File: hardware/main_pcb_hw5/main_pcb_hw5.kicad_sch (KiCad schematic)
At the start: 25 parts, among them J1 MEGA BOTTOM, J10 GBA_Slot, J3 CART SLOT TOP ROW, J4 CART SLOT FRONT ROW, J6 5V USB, J7 Conn_01x07, J8 EXP2, J9 EXP1, M2_1 Screw_Terminal_01x01, M2_2 Screw_Terminal_01x01, M2_3 Screw_Terminal_01x01, M2_4 Screw_Terminal_01x01, M2_5 Screw_Terminal_01x01, M2_6 Screw_Terminal_01x01, M2_7 Screw_Terminal_01x01, M2_8 Screw_Terminal_01x01, M2_9 Screw_Terminal_01x01, SW1 VOLTAGE, SW2 POWER, U2 DS3231MZ

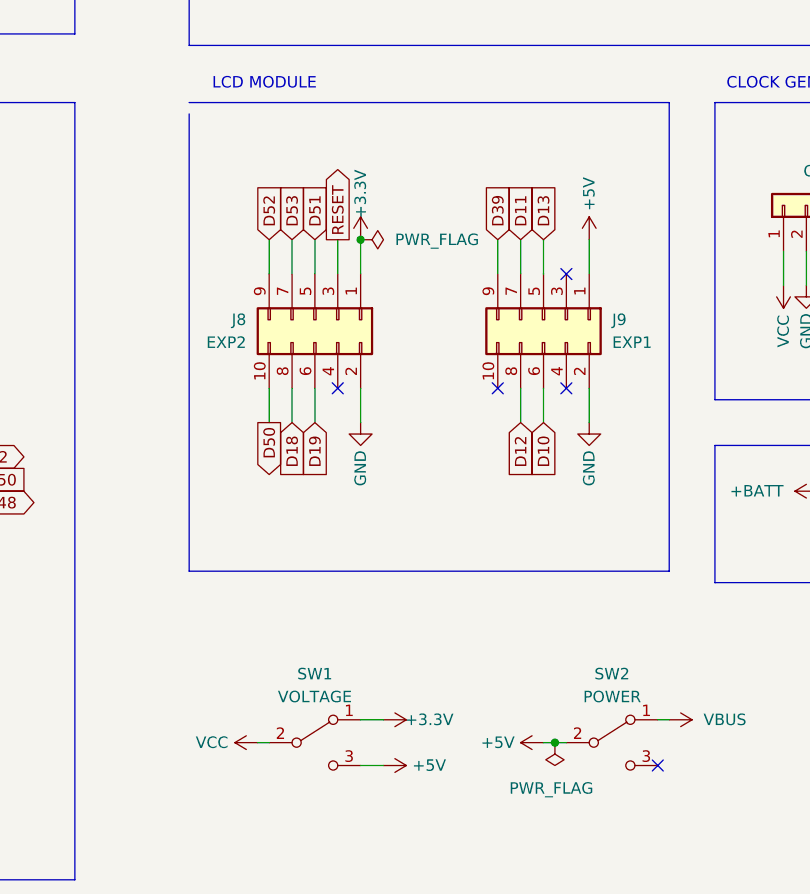
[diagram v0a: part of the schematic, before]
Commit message: Changed 0402 components to 0603
 - Also tweaked name in board graphics to make it clear this isn't a
   vanilla board.
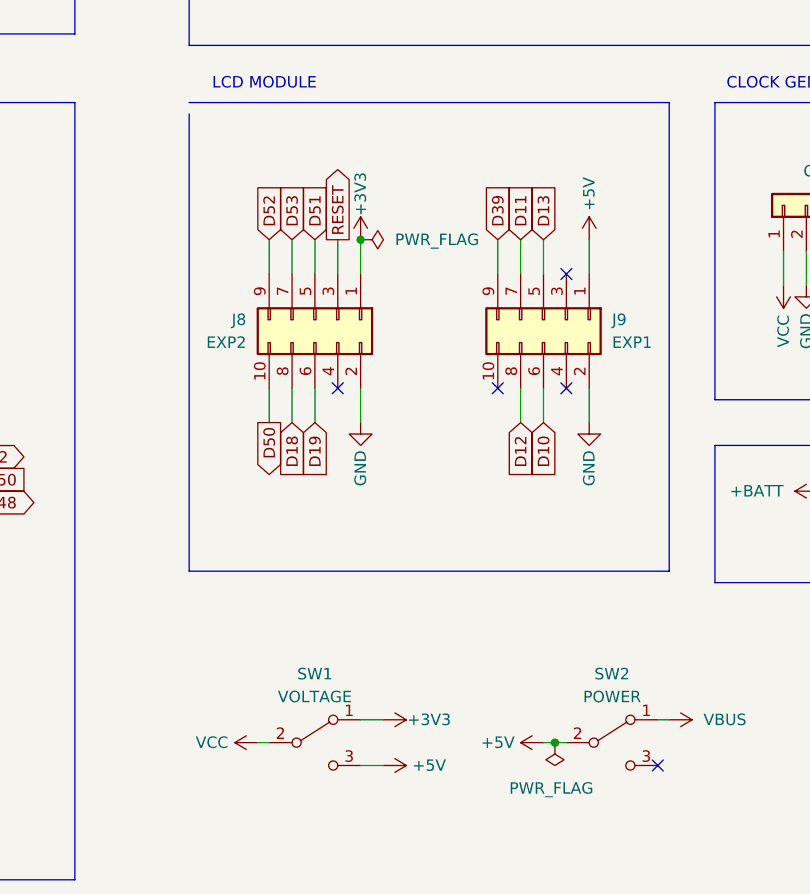
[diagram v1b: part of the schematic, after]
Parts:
- C5: footprint Capacitor_SMD:C_0402_1005Metric_Pad0.74x0.62mm_HandSolder -> Capacitor_SMD:C_0603_1608Metric_Pad1.08x0.95mm_HandSolder

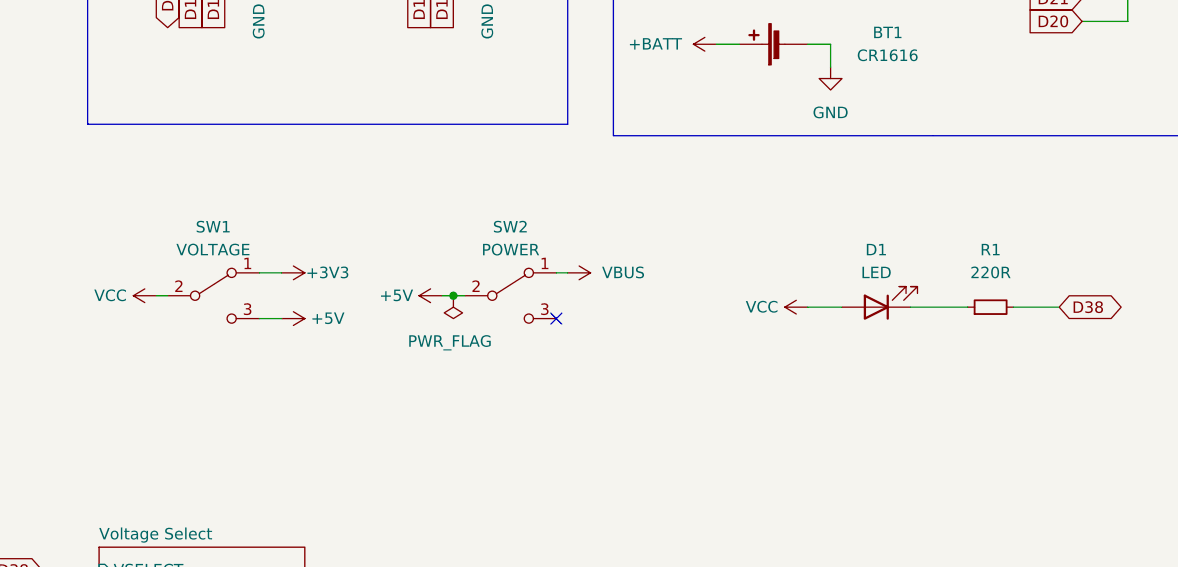
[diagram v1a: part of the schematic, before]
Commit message: Made LED and its resistor SMD, added teardrops
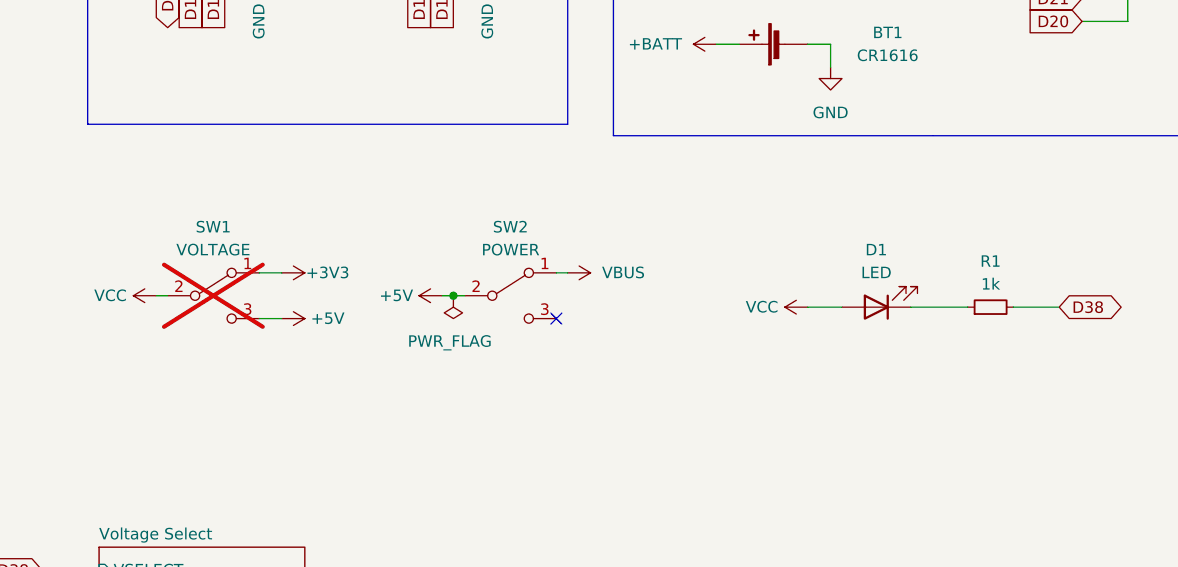
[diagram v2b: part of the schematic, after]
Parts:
- D1: footprint LED_THT:LED_D3.0mm -> LED_SMD:LED_0603_1608Metric_Pad1.05x0.95mm_HandSolder
- M2_1, M2_2, M2_3, M2_4, M2_5, M2_6, M2_7, M2_8, M2_9: footprint (none) -> MountingHole:MountingHole_2.2mm_M2_ISO7380_Pad
- R1: value 220R -> 1k; footprint Resistor_THT:R_Axial_DIN0207_L6.3mm_D2.5mm_P10.16mm_Horizontal -> Resistor_SMD:R_0603_1608Metric_Pad0.98x0.95mm_HandSolder
- SW1: now not fitted
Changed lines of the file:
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@@
 			)
 		)
-		(property "Footprint" ""
+		(property "Footprint" "MountingHole:MountingHole_2.2mm_M2_ISO7380_Pad"
 			(at 254 55.88 0)
 			(effects
@@
 			)
 		)
-		(property "Footprint" ""
+		(property "Footprint" "MountingHole:MountingHole_2.2mm_M2_ISO7380_Pad"
 			(at 254 45.72 0)
 			(effects
@@
 			)
 		)
-		(property "Footprint" ""
+		(property "Footprint" "MountingHole:MountingHole_2.2mm_M2_ISO7380_Pad"
 			(at 254 30.48 0)
 			(effects
@@
 			)
 		)
-		(property "Footprint" ""
+		(property "Footprint" "MountingHole:MountingHole_2.2mm_M2_ISO7380_Pad"
 			(at 254 40.64 0)
 			(effects
@@
 			)
 		)
-		(property "Footprint" ""
+		(property "Footprint" "MountingHole:MountingHole_2.2mm_M2_ISO7380_Pad"
 			(at 254 60.96 0)
 			(effects
@@
 			)
 		)
-		(property "Footprint" ""
+		(property "Footprint" "MountingHole:MountingHole_2.2mm_M2_ISO7380_Pad"
 			(at 254 35.56 0)
 			(effects
@@
 			)
 		)
-		(property "Footprint" ""
+		(property "Footprint" "MountingHole:MountingHole_2.2mm_M2_ISO7380_Pad"
 			(at 254 50.8 0)
 			(effects
@@
 		(fields_autoplaced yes)
 		(property "Reference" "R1"
-			(at 247.65 147.32 90)
+			(at 247.65 148.59 90)
 			(effects
 				(font
@@
 			)
 		)
-		(property "Value" "220R"
-			(at 247.65 149.86 90)
+		(property "Value" "1k"
+			(at 247.65 151.13 90)
 			(effects
 				(font
@@
 			)
 		)
-		(property "Footprint" "Resistor_THT:R_Axial_DIN0207_L6.3mm_D2.5mm_P10.16mm_Horizontal"
+		(property "Footprint" "Resistor_SMD:R_0603_1608Metric_Pad0.98x0.95mm_HandSolder"
 			(at 247.65 153.67 0)
 			(effects
@@
 			)
 		)
+		(property "Digikey Product Number" ""
+			(at 247.65 153.67 0)
+			(effects
+				(font
+					(size 1.27 1.27)
+				)
+				(hide yes)
+			)
+		)
+		(property "Manufacturer Product Number" ""
+			(at 247.65 153.67 0)
+			(effects
+				(font
+					(size 1.27 1.27)
+				)
+				(hide yes)
+			)
+		)
 		(pin "1"
 		)
@@
 			)
 		)
-		(property "Footprint" ""
+		(property "Footprint" "MountingHole:MountingHole_2.2mm_M2_ISO7380_Pad"
 			(at 254 25.4 0)
 			(effects
@@
 		(in_bom yes)
 		(on_board yes)
-		(dnp no)
+		(dnp yes)
 		(fields_autoplaced yes)
 		(property "Reference" "SW1"
@@
 			)
 		)
+		(property "Digikey Product Number" ""
+			(at 161.29 152.4 0)
+			(effects
+				(font
+					(size 1.27 1.27)
+				)
+				(hide yes)
+			)
+		)
+		(property "Manufacturer Product Number" ""
+			(at 161.29 152.4 0)
+			(effects
+				(font
+					(size 1.27 1.27)
+				)
+				(hide yes)
+			)
+		)
 		(pin "1"
 		)
@@
 			)
 		)
-		(property "Footprint" "LED_THT:LED_D3.0mm"
+		(property "Footprint" "LED_SMD:LED_0603_1608Metric_Pad1.05x0.95mm_HandSolder"
 			(at 234.95 153.67 0)
 			(effects
@@
 			)
 		)
+		(property "Digikey Product Number" ""
+			(at 234.95 153.67 0)
+			(effects
+				(font
+					(size 1.27 1.27)
+				)
+				(hide yes)
+			)
+		)
+		(property "Manufacturer Product Number" ""
+			(at 234.95 153.67 0)
+			(effects
+				(font
+					(size 1.27 1.27)
+				)
+				(hide yes)
+			)
+		)
 		(pin "1"
 		)
@@
 			)
 		)
-		(property "Footprint" ""
+		(property "Footprint" "MountingHole:MountingHole_2.2mm_M2_ISO7380_Pad"
 			(at 254 20.32 0)
 			(effects
